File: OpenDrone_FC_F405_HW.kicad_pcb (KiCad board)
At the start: 8 copper layers, 34 x 34 mm, 106 parts, among them J1 Conn_01x05, J10 Conn_01x02, J12 Conn_01x02, J13 Conn_01x02, J14 Conn_01x02, J15 Conn_01x02, J16 Conn_01x02, J17 Conn_01x02, J19 Conn_01x02, J2 Conn_01x02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

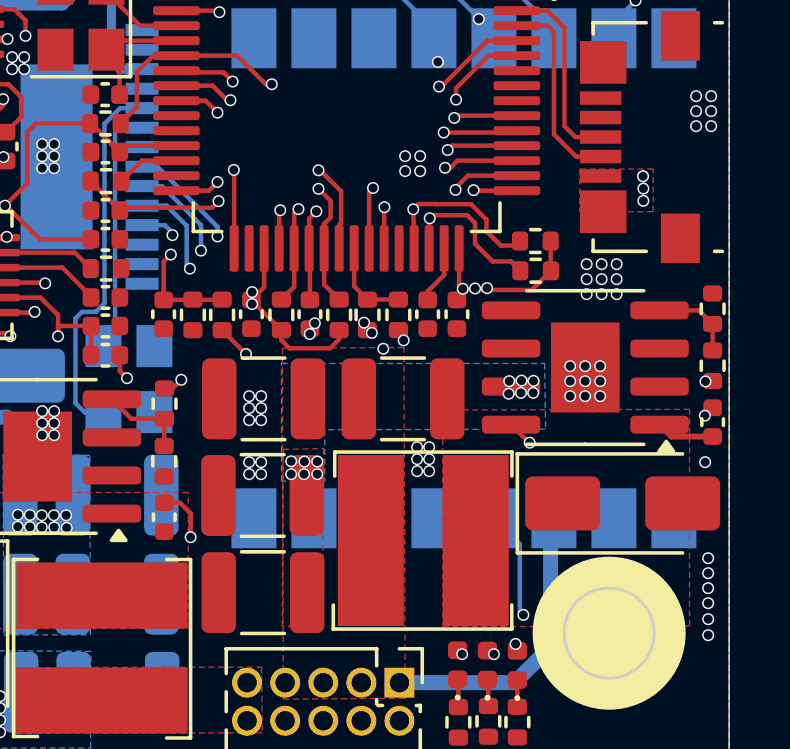
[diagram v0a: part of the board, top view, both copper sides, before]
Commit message: add LoRa IRQ
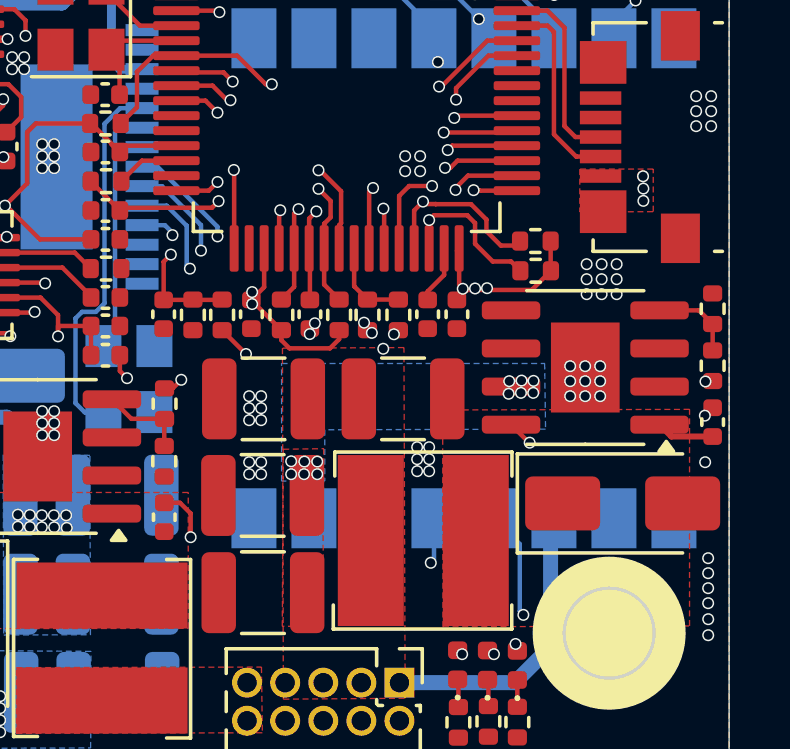
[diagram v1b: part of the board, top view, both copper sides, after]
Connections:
- U1 pad 28: unconnected-(U1-PB2-Pad28) -> LORA_IRQ
- U9 pad 5: unconnected-(U9-DIO0-Pad5) -> LORA_IRQ
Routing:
- net LORA_IRQ: track 0.00 -> 19.5 mm, vias 0 -> 2
- net LORA_RST: track 33.4 -> 35.7 mm
- net LED_GREEN: track 28.6 -> 30.6 mm
- net LED_BLUE: track 27.9 -> 29.4 mm
- net SPI3_MISO: track 36.5 -> 37.5 mm

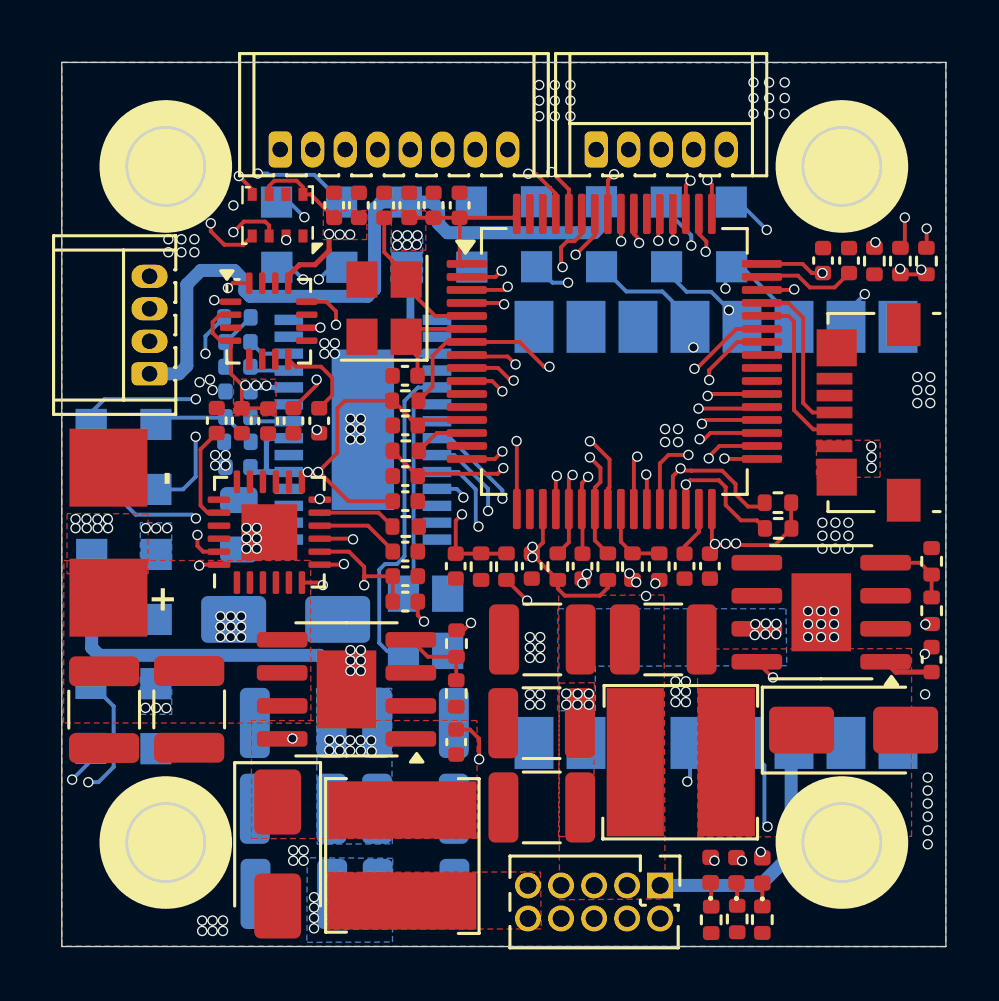
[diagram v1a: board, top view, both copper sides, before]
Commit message: use mpu6050 and change spi pinout
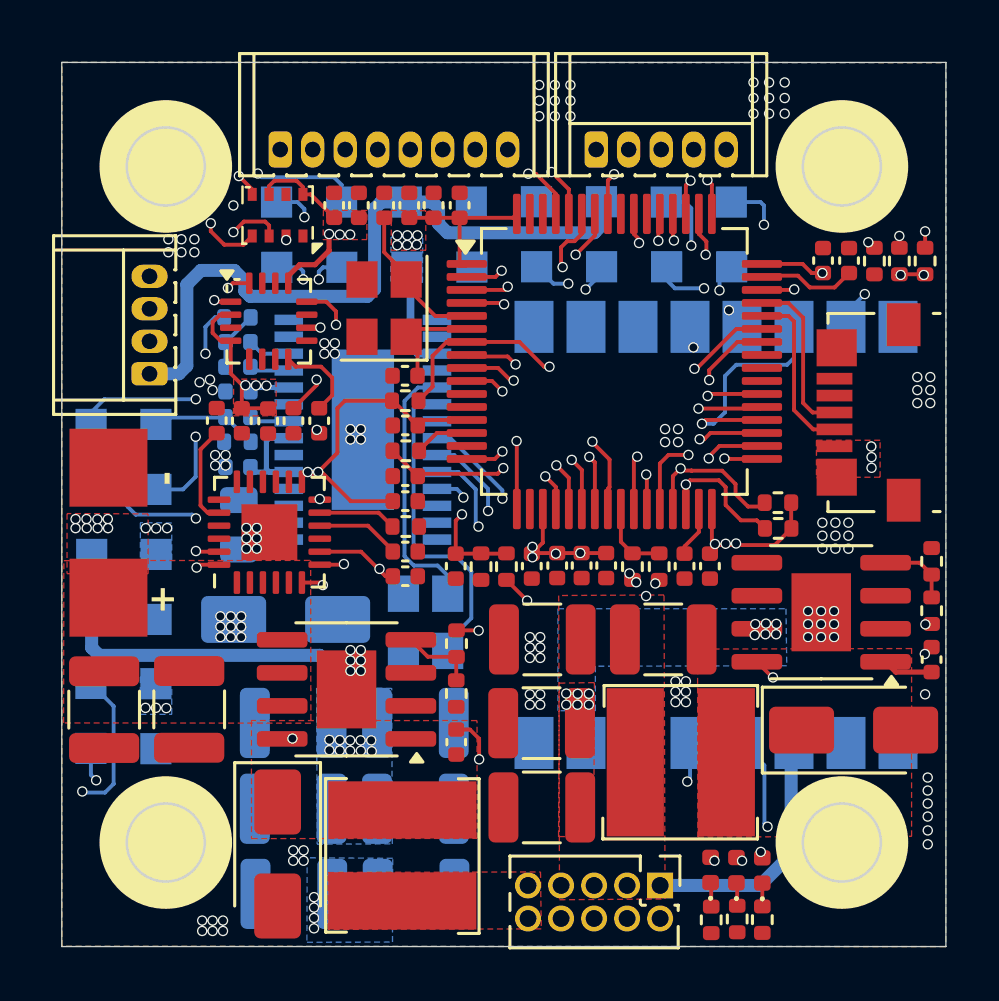
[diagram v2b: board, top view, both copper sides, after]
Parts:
- removed R12, R13: TBD, Capacitor_SMD:C_0402_1005Metric
- removed R23, R24: 4.7k, Resistor_SMD:R_0402_1005Metric
- added C44: 100nF, Capacitor_SMD:C_0402_1005Metric, F.Cu at (154.4, 85.6)
- added C45: 100nF, Capacitor_SMD:C_0402_1005Metric, F.Cu at (153.5, 85.6)
- added C46: 100nF, Capacitor_SMD:C_0402_1005Metric, F.Cu at (152.6, 85.6)
- moved R8 17.6 mm to (165.7, 73.9)
- moved R7 16.9 mm to (166.7, 73.9)
- turned Y2 to -90 degrees
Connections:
- C19 pad 1: MPU6000_CS -> +3V3
- J7 pad 1: SPI2_CS -> SPI1_CS
- J7 pad 2: SPI2_CLK -> SPI1_CLK
- J7 pad 3: SPI2_MISO -> SPI1_MISO
- J7 pad 4: SPI2_MOSI -> SPI1_MOSI
- R7 pad 2: MPU6000_MOSI -> I2C1_SDA
- R8 pad 2: MPU6000_CLK -> I2C1_SCL
- U1 pad 20: MPU6000_CS -> SPI1_CS
- U1 pad 21: MPU6000_CLK -> SPI1_CLK
- U1 pad 22: MPU6000_MISO -> SPI1_MISO
- U1 pad 23: MPU6000_MOSI -> SPI1_MOSI
- U1 pad 56: LORA_CS -> unconnected-(U1-PB4-Pad56)
- U4 pad 23: MPU6000_CLK -> I2C1_SCL
- U4 pad 24: MPU6000_MOSI -> I2C1_SDA
- U4 pad 8: MPU6000_CS -> +3V3
- U4 pad 9: MPU6000_MISO -> GND
- U9 pad 15: LORA_CS -> SPI2_CS
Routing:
- net MPU6000_MOSI: track 24.3 -> 0.00 mm, vias 2 -> 0
- net I2C1_SDA: track 19.7 -> 42.8 mm, vias 3 -> 4
- net I2C1_SCL: track 18.6 -> 41.1 mm, vias 3 -> 4
- net MPU6000_CLK: track 22.2 -> 0.00 mm, vias 2 -> 0
- net MPU6000_CS: track 15.7 -> 0.00 mm, vias 2 -> 0
- net MPU6000_MISO: track 15.5 -> 0.00 mm, vias 2 -> 0
- net SPI1_MISO: track 0.00 -> 15.4 mm, vias 0 -> 2
- net SPI1_MOSI: track 0.00 -> 15.2 mm, vias 0 -> 2
- net LORA_CS: track 14.1 -> 0.00 mm, vias 2 -> 0
- net SPI1_CS: track 0.00 -> 10.8 mm, vias 0 -> 2
- net SPI1_CLK: track 0.00 -> 10.4 mm, vias 0 -> 2
- net SPI2_CLK: track 12.3 -> 7.73 mm
- net SPI2_MISO: track 12.4 -> 8.38 mm
- net SPI2_MOSI: track 12.9 -> 8.97 mm, vias 2 -> 1
- net Net-(U7-XFB): track 9.02 -> 12.4 mm
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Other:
- board text added: "CLK1"
- board text added: "CS1"
- board text added: "MI1"
- board text added: "MO1"
- board text removed: "CLK2"
- board text removed: "CS2"
- board text removed: "MI2"
- board text removed: "MO2"
